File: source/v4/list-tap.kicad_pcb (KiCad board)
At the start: 2 copper layers, 30 x 33 mm, 52 parts, among them J1 WURTH_61300411121, J2 WURTH_61300411121, SW1 SKRKAEE020, SW2 SKRKAEE020, SW3 PTS815 SJM 250 SMTR LFS, U1 ESP32-C3-MINI-1-N4, U3 USBLC6-2SC6Y, U5 TPS63805YFFR

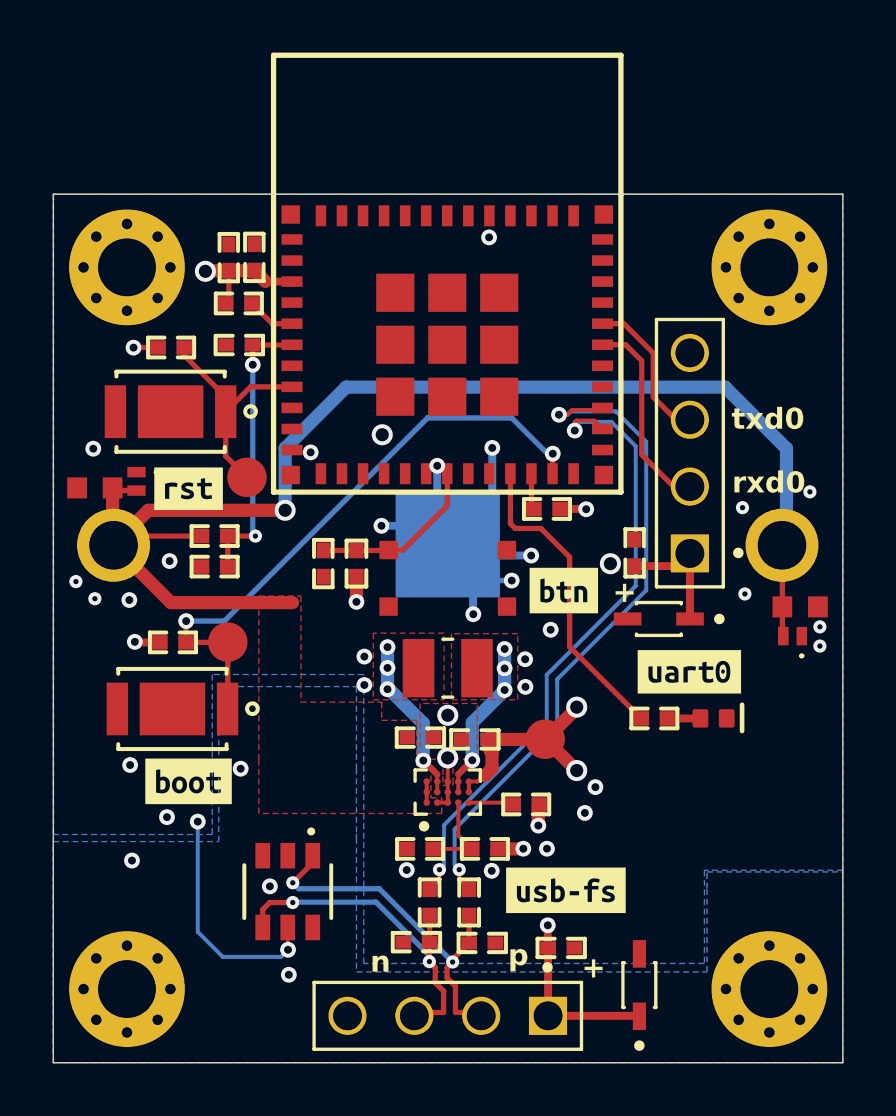
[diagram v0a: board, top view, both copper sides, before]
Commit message: rounded corners, DRC checks
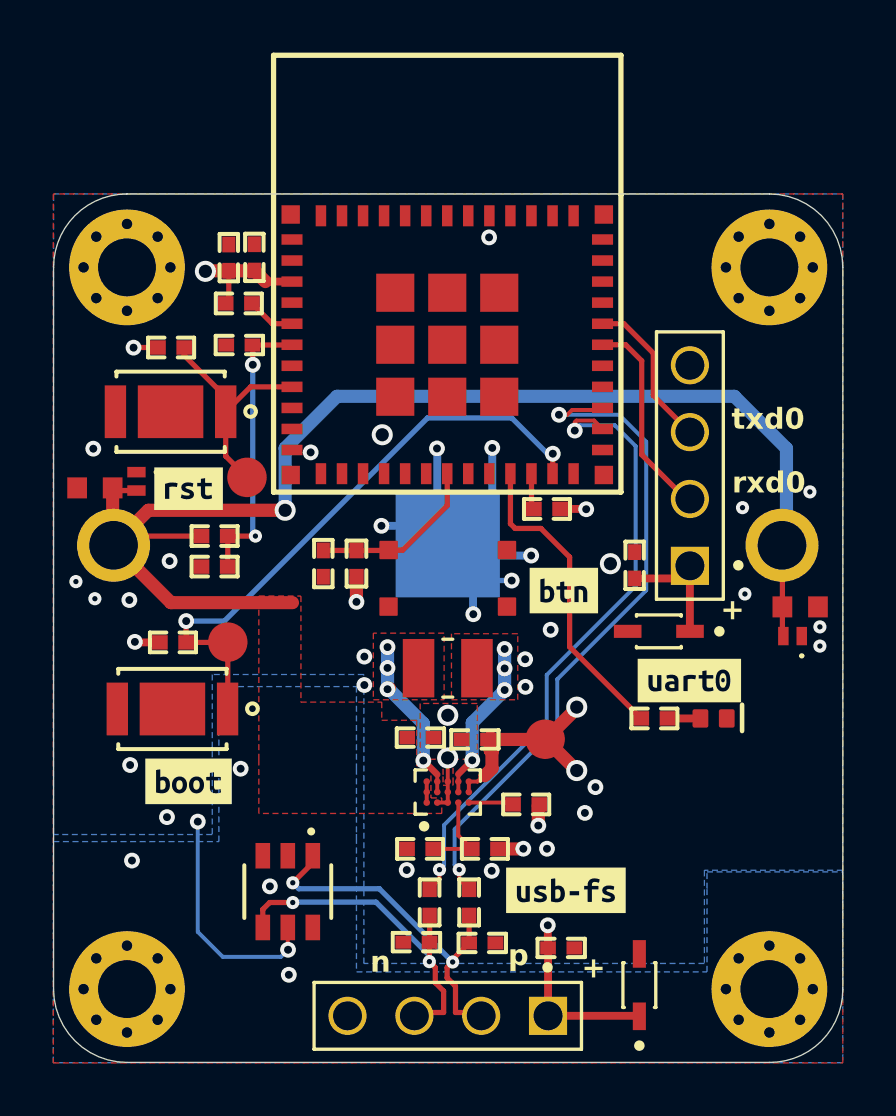
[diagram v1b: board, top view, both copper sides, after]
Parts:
- moved C17 0.47 mm to (159.3, 74.0)
- moved D1 0.47 mm to (160.3, 76.5)
- moved J1 0.47 mm to (161.4, 70.2)
- moved kibuzzard-6AE057F3 0.33 mm to (161.4, 78.4)
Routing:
- net GND: track 26.7 -> 27.3 mm
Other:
- outline, holes or cut-outs redrawn
